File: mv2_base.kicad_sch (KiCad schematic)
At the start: 55 parts, among them J1 Conn_01x20, J2 OLED, U1 TPS65130RGE

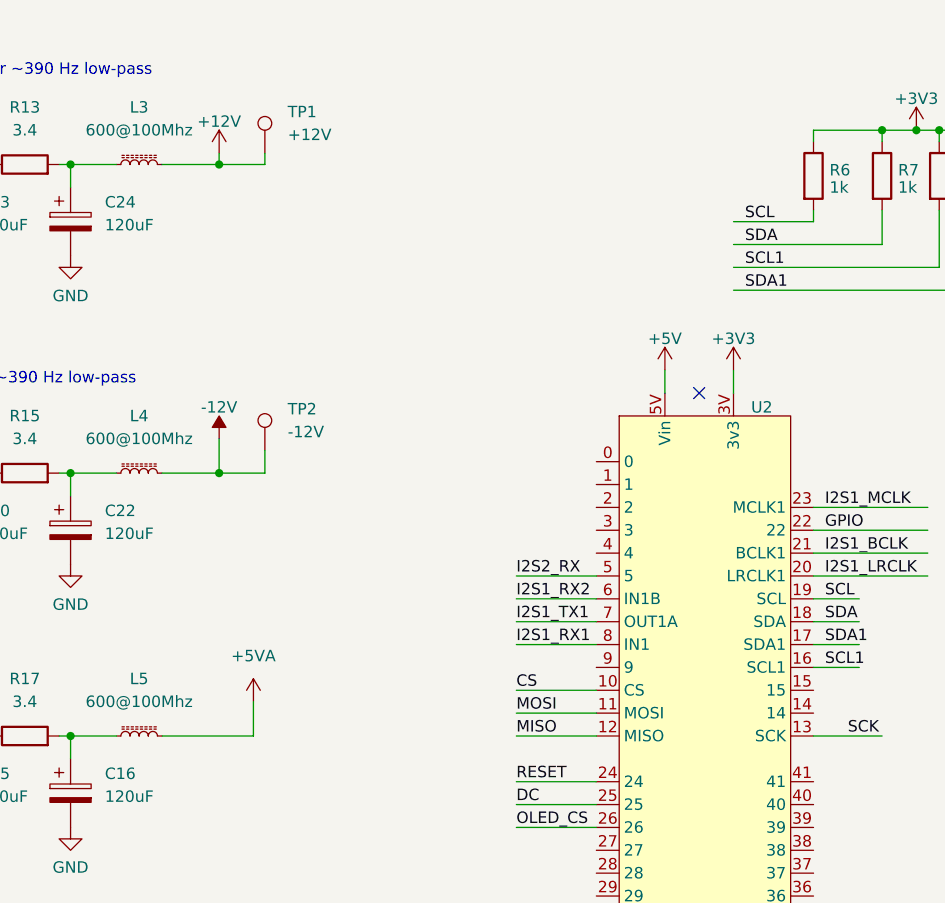
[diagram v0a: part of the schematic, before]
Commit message: Add jumpers in power rails and more test points
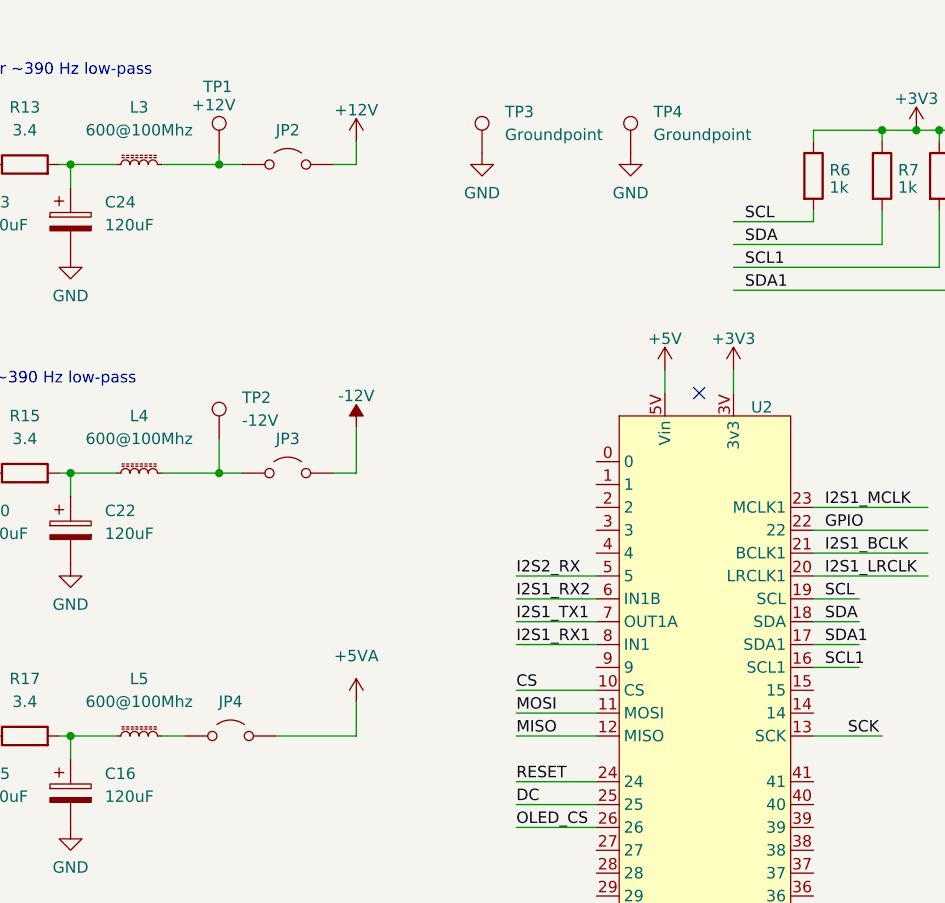
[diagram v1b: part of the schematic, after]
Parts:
- added JP2, JP3, JP4: Jumper_2_Open, Connector_PinHeader_2.54mm:PinHeader_1x02_P2.54mm_Vertical, symbol Jumper:Jumper_2_Open
- added TP3, TP4: Groundpoint, TestPoint:TestPoint_Bridge_Pitch2.54mm_Drill1.0mm, symbol Connector:TestPoint
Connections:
- net +12V: now also JP2.2 (B); no longer L3.2, TP1.1
- net +5VA: now also JP4.2 (B); no longer L5.2
- net -12V: now also JP3.2 (B); no longer L4.2, TP2.1
- net GND: now also TP3.1, TP4.1
- new net: JP2.1 (A), L3.2, TP1.1
- new net: JP4.1 (A), L5.2
- new net: JP3.1 (A), L4.2, TP2.1

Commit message: New filters
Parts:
- removed C15, C16, C20, C22, C23, C24: 120uF, Capacitor_SMD:CP_Elec_6.3x7.7, symbol Device:C_Polarized
- removed JP4: Jumper_2_Open, Connector_PinHeader_2.54mm:PinHeader_1x02_P2.54mm_Vertical, symbol Jumper:Jumper_2_Open
- removed L3, L4: 600@100Mhz, Inductor_SMD:L_0603_1608Metric, symbol Device:L_Ferrite_Small
- added C13: 33nF, Capacitor_SMD:C_0603_1608Metric_Pad1.08x0.95mm_HandSolder, symbol Device:C_Small
- added C14: 330pF, Capacitor_SMD:C_0603_1608Metric_Pad1.08x0.95mm_HandSolder, symbol Device:C_Small
- added C15: 12nF, Capacitor_SMD:C_0603_1608Metric_Pad1.08x0.95mm_HandSolder, symbol Device:C_Small
- added C16: 1uF, Capacitor_SMD:C_0805_2012Metric_Pad1.18x1.45mm_HandSolder, symbol Device:C_Small
- added C17, C18: 0.1uF, Capacitor_SMD:C_0402_1005Metric, symbol Device:C_Small
- added C25, C26, C27, C28, C29, C30: 22uF, Capacitor_SMD:C_0805_2012Metric, symbol Device:C_Polarized
- added D3, D4, D5, D6: B5819W SL, Diode_SMD:D_SOD-123, symbol Device:D_Schottky
- added L3: 4.7uH, Inductor_SMD:L_Wuerth_WE-TPC-3816, symbol Device:L_Iron
- added L6, L7: 600@100Mhz, Inductor_SMD:L_0603_1608Metric, symbol Device:L_Ferrite_Small
- added Q1: SS8550, Package_TO_SOT_SMD:SOT-23, symbol Transistor_BJT:Q_PNP_BEC
- added Q2, Q3: S8050, Package_TO_SOT_SMD:SOT-23, symbol Transistor_BJT:Q_NPN_BEC
- added R18: 500, Resistor_SMD:R_0402_1005Metric, symbol Device:R
- added R19: 21.5k, Resistor_SMD:R_0402_1005Metric, symbol Device:R
- added U3: LM5158, symbol Library:LM5158
- C19: footprint Capacitor_SMD:C_0805_2012Metric_Pad1.18x1.45mm_HandSolder -> Capacitor_SMD:C_0805_2012Metric; DatasheetRef C4 -> C5
- R12: value 3.4 -> 100k; footprint Resistor_SMD:R_0603_1608Metric -> Resistor_SMD:R_0402_1005Metric; LCSC C22939 -> C25803; Part R 3.4Ω 125mW 1% 0603 -> (none); Shop https://eu.mouser.com/ProductDetail/YAGEO/RC0603FR-073R4L?q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 -> (none)
- R13: value 3.4 -> 2.49k; footprint Resistor_SMD:R_0603_1608Metric -> Resistor_SMD:R_0402_1005Metric; LCSC C22939 -> C25803; Part R 3.4Ω 125mW 1% 0603 -> (none); Shop https://eu.mouser.com/ProductDetail/YAGEO/RC0603FR-073R4L?q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 -> (none)
- R14: value 3.4 -> 118k; footprint Resistor_SMD:R_0603_1608Metric -> Resistor_SMD:R_0402_1005Metric; LCSC C22939 -> C25803; Part R 3.4Ω 125mW 1% 0603 -> (none); Shop https://eu.mouser.com/ProductDetail/YAGEO/RC0603FR-073R4L?q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 -> (none)
- R15: value 3.4 -> 1.58k; footprint Resistor_SMD:R_0603_1608Metric -> Resistor_SMD:R_0402_1005Metric; LCSC C22939 -> C25803; Part R 3.4Ω 125mW 1% 0603 -> (none); Shop https://eu.mouser.com/ProductDetail/YAGEO/RC0603FR-073R4L?q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 -> (none)
- R16, R17: value 3.4 -> 500; footprint Resistor_SMD:R_0603_1608Metric -> Resistor_SMD:R_0402_1005Metric; LCSC C22939 -> (none); Part R 3.4Ω 125mW 1% 0603 -> (none); Shop https://eu.mouser.com/ProductDetail/YAGEO/RC0603FR-073R4L?q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 -> (none)
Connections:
- net +5V: now also C18.1, L3.2, L7.1, U3.3 (BIAS); no longer R16.1
- net +5VA: now also C30.1, D5.2 (A), Q3.2 (E)
- net GND: now also R12.1, R13.1, C13.2, C14.2, C15.2, C16.2, C17.2, C18.2, C25.2, C26.2, C27.1, C28.1, C29.2, C30.2, R19.1, U3.1 (PGND), U3.16 (PGND), U3.7 (AGND)
- net VNEG: now also L6.1; no longer R14.1
- net at R15.1: now also C13.1; no longer R14.2
- net at JP2.1 (A), TP1.1: now also C26.1, D3.2 (A), Q2.2 (E)
- net at R16.2: now also C25.1, D3.1 (K), Q2.1 (B); no longer R17.1
- net at L5.2: now also R16.1, Q2.3 (C)
- net at R13.2: now also R14.1, U3.9 (FB)
- net at JP3.1 (A), TP2.1: now also C28.2, D4.2 (A), Q1.2 (E)
- net at R17.2: now also L6.2, Q1.3 (C); no longer L5.1
- net at C3.1, C4.1, D1.1 (K)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: now also L5.1; no longer C19.1, R12.1
- net at R12.2: now also U3.11 (MODE); no longer R13.1
- net at R15.2: now also C14.1, U3.8 (COMP)
- new net: L7.2, Q3.3 (C), R18.1
- new net: C15.1, U3.10 (SS)
- new net: D6.2 (A), L3.1, U3.13 (SW), U3.14 (SW)
- new net: C16.1, U3.2 (VCC)
- new net: R19.2, U3.5 (RT)
- new net: C17.1, C19.1, D6.1 (K), R14.2
- new net: C29.1, D5.1 (K), Q3.1 (B), R18.2
- new net: C27.2, D4.1 (K), Q1.1 (B), R17.1
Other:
- note removed: "2 stage RC filter ~390 Hz low-pass"
- moved on the sheet: C1, C10, C11, C12, C2, C21, C3, C4, C5, C6, C7, C8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

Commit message: Implement +48V supply
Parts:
- added C20: 10uF, Capacitor_SMD:C_0805_2012Metric_Pad1.18x1.45mm_HandSolder, symbol Device:C_Small
- added L8: 600@100Mhz, Inductor_SMD:L_0603_1608Metric, symbol Device:L_Ferrite_Small
- C13: footprint Capacitor_SMD:C_0603_1608Metric_Pad1.08x0.95mm_HandSolder -> Capacitor_SMD:C_0603_1608Metric; LCSC C14663 -> C21117
- C14: footprint Capacitor_SMD:C_0603_1608Metric_Pad1.08x0.95mm_HandSolder -> Capacitor_SMD:C_0603_1608Metric; LCSC C14663 -> C1664
- C15: value 12nF -> 22nF; footprint Capacitor_SMD:C_0603_1608Metric_Pad1.08x0.95mm_HandSolder -> Capacitor_SMD:C_0402_1005Metric; LCSC C14663 -> C1532
- C16: footprint Capacitor_SMD:C_0805_2012Metric_Pad1.18x1.45mm_HandSolder -> Capacitor_SMD:C_0402_1005Metric; LCSC C15850 -> C52923
- C18: LCSC C14663 -> C307331
- C19: Note Low ESR -> (none)
- D6: value B5819W SL -> SS210; footprint Diode_SMD:D_SOD-123 -> Diode_SMD:D_SMA; LCSC C8598 -> C14996
- R12: LCSC C25803 -> C25879
- R13: value 2.49k -> 2.2k; LCSC C25803 -> C25741
- R14: value 118k -> 100k; LCSC C25803 -> C25879
- R15: value 1.58k -> 1.5k; LCSC C25803 -> C25867
- R19: value 21.5k -> 22k; LCSC C25803 -> C25768
- U3: footprint (none) -> Package_DFN_QFN:WQFN-16-1EP_3x3mm_P0.5mm_EP1.68x1.68mm_ThermalVias
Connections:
- net +5V: now also U3.6 (EN), C20.1
- net GND: now also C20.2
- net SW: now reaches D6.2 (A), L3.1, U3.13 (SW), U3.14 (SW)
- net 12VREG: now reaches C3.1, C4.1, D1.1 (K), L5.1, R1.2, R11.1, U1.23 (VPOS)
- net 48VREG: now reaches C17.1, C19.1, D6.1 (K), R14.2
- net 48VREG: now also L8.1
- net GPIO: no longer names the net of U2.22
- net GPIO: no longer J1.1 (Pin_1)
- net VNEG renamed 12NREG
- new net +48V: J1.1 (Pin_1), L8.2
- no-connect marks 2 -> 3
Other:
- moved on the sheet: C13, C14, C15, C16, C17, C18, C19, D6, H1, H2, H3, H4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

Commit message: Fix up some LCSC part numbers
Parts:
- C10, C17, C7: LCSC C14663 -> C307331
- R12, R14: LCSC C25879 -> C25741
- R3: LCSC C25803 -> C25741
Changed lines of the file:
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@@
 			)
 		)
-		(property "LCSC" "C25803"
+		(property "LCSC" "C25741"
 			(at 78.74 63.5 0)
 			(effects
@@
 			)
 		)
-		(property "LCSC" "C14663"
+		(property "LCSC" "C307331"
 			(at 111.76 85.09 0)
 			(effects
@@
 			)
 		)
-		(property "LCSC" "C25879"
+		(property "LCSC" "C25741"
 			(at 107.95 154.94 0)
 			(effects
@@
 			)
 		)
-		(property "LCSC" "C14663"
+		(property "LCSC" "C307331"
 			(at 120.65 151.13 0)
 			(effects
@@
 			)
 		)
-		(property "LCSC" "C14663"
+		(property "LCSC" "C307331"
 			(at 41.91 72.39 0)
 			(effects
@@
 			)
 		)
-		(property "LCSC" "C25879"
+		(property "LCSC" "C25741"
 			(at 102.87 182.88 0)
 			(effects

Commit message: Fix up some LCSC part numbers
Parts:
- C11: LCSC C57112 -> C15195
- C12: LCSC C53987 -> C1538
- C19, C21, C4, C9: LCSC C15850 -> C1779
- C2: LCSC C1653 -> C1555
- R1: value 240k -> 200k; LCSC C4197 -> C25768
- R13: LCSC C25741 -> C25879
- R2: value 27k -> 24k; LCSC C22967 -> C25764
- R4: LCSC C22775 -> C25076
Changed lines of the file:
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@@
 			)
 		)
-		(property "LCSC" "C25741"
+		(property "LCSC" "C25879"
 			(at 107.95 165.1 0)
 			(effects
@@
 			)
 		)
-		(property "LCSC" "C53987"
+		(property "LCSC" "C1538"
 			(at 86.36 92.71 0)
 			(effects
@@
 			)
 		)
-		(property "LCSC" "C15850"
+		(property "LCSC" "C1779"
 			(at 132.08 151.13 0)
 			(effects
@@
 			)
 		)
-		(property "Value" "240k"
+		(property "Value" "200k"
 			(at 104.648 50.8073 0)
 			(effects
@@
 			)
 		)
-		(property "LCSC" "C4197"
+		(property "LCSC" "C25768"
 			(at 102.87 49.53 0)
 			(effects
@@
 			)
 		)
-		(property "LCSC" "C22775"
+		(property "LCSC" "C25076"
 			(at 36.83 66.04 0)
 			(effects
@@
 			)
 		)
-		(property "LCSC" "C15850"
+		(property "LCSC" "C1779"
 			(at 121.92 85.09 0)
 			(effects
@@
 			)
 		)
-		(property "LCSC" "C15850"
+		(property "LCSC" "C1779"
 			(at 133.35 85.09 0)
 			(effects
@@
 			)
 		)
-		(property "LCSC" "C15850"
+		(property "LCSC" "C1779"
 			(at 130.81 49.53 0)
 			(effects
@@
 			)
 		)
-		(property "Value" "27k"
+		(property "Value" "24k"
 			(at 104.648 62.2373 0)
 			(effects
@@
 			)
 		)
-		(property "LCSC" "C22967"
+		(property "LCSC" "C25764"
 			(at 102.87 60.96 0)
 			(effects
@@
 			)
 		)
-		(property "LCSC" "C1653"
+		(property "LCSC" "C1555"
 			(at 111.76 53.34 0)
 			(effects
@@
 			)
 		)
-		(property "LCSC" "C57112"
+		(property "LCSC" "C15195"
 			(at 77.47 92.71 0)
 			(effects

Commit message: Fix up some LCSC part numbers
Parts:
- C5: LCSC C21120 -> C16772
- C8: value 7.5pF -> 10pF; LCSC C15850 -> C32949
- R1: LCSC C25768 -> C25764
- R2: value 24k -> 22k; LCSC C25764 -> C25768
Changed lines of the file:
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@@
 			)
 		)
-		(property "LCSC" "C25768"
+		(property "LCSC" "C25764"
 			(at 102.87 49.53 0)
 			(effects
@@
 			)
 		)
-		(property "LCSC" "C21120"
+		(property "LCSC" "C16772"
 			(at 86.36 60.96 0)
 			(effects
@@
 			)
 		)
-		(property "Value" "7.5pF"
+		(property "Value" "10pF"
 			(at 86.36 71.628 90)
 			(effects
@@
 			)
 		)
-		(property "LCSC" "C15850"
+		(property "LCSC" "C32949"
 			(at 86.36 68.58 0)
 			(effects
@@
 			)
 		)
-		(property "Value" "24k"
+		(property "Value" "22k"
 			(at 104.648 62.2373 0)
 			(effects
@@
 			)
 		)
-		(property "LCSC" "C25764"
+		(property "LCSC" "C25768"
 			(at 102.87 60.96 0)
 			(effects

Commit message: Replace 500ohm resistor with 510ohm basic part
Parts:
- R16, R17, R18: value 500 -> 510; LCSC (none) -> C25123
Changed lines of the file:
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@@
 			)
 		)
-		(property "Value" "500"
+		(property "Value" "510"
 			(at 158.75 49.5299 0)
 			(effects
@@
 			)
 		)
+		(property "LCSC" "C25123"
+			(at 156.21 48.26 0)
+			(effects
+				(font
+					(size 1.27 1.27)
+				)
+				(hide yes)
+			)
+		)
 		(pin "1"
 		)
@@
 			)
 		)
-		(property "Value" "500"
+		(property "Value" "510"
 			(at 158.75 115.5699 0)
 			(effects
@@
 			)
 		)
+		(property "LCSC" "C25123"
+			(at 156.21 114.3 0)
+			(effects
+				(font
+					(size 1.27 1.27)
+				)
+				(hide yes)
+			)
+		)
 		(pin "1"
 		)
@@
 			)
 		)
-		(property "Value" "500"
+		(property "Value" "510"
 			(at 158.75 76.1999 0)
 			(effects
@@
 			(at 156.21 74.93 0)
 			(effects
+				(font
+					(size 1.27 1.27)
+				)
+				(hide yes)
+			)
+		)
+		(property "LCSC" "C25123"
+			(at 156.21 74.93 0)
+			(effects
